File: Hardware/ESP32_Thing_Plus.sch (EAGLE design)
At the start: 43 parts, among them Q1 2.5A/30V, Q2 MBT3904DW1T1, U1 MCP73831, U2 ESP-WROOM-32NARROW, U3 AP2112K-3.3V, U4 CP2102N

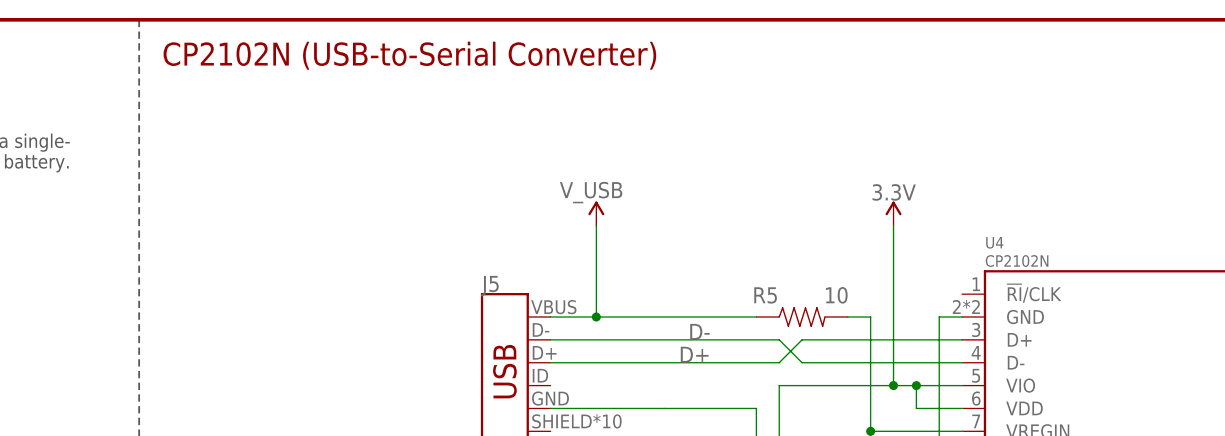
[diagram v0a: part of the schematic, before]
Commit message: Updated USB to UART converter
Updated shematic to indicate the USB to UART converter can be either the CP2104 or CP2102N
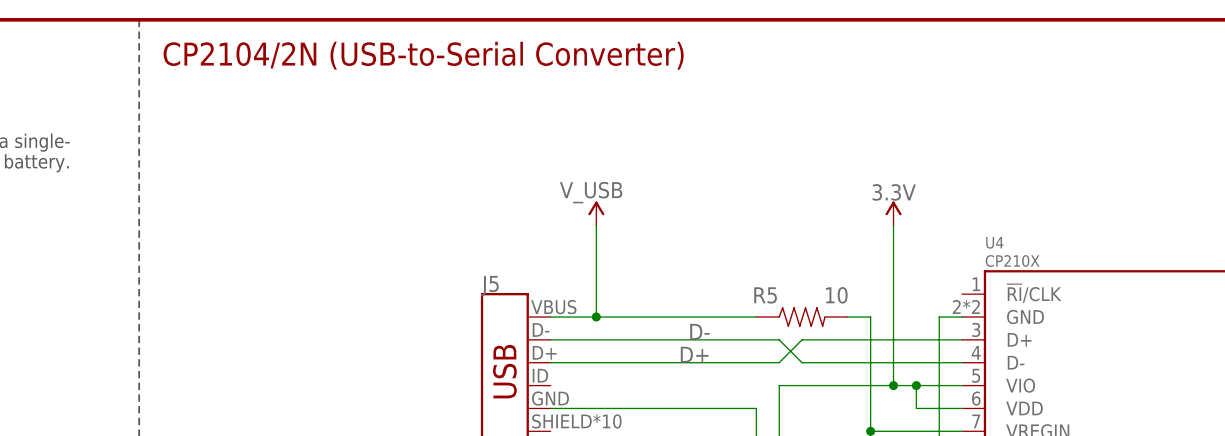
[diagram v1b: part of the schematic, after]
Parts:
- U4: value CP2102N -> CP210X
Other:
- note added: "CP2104/2N (USB-to-Serial Converter)"
- note removed: "CP2102N (USB-to-Serial Converter)"
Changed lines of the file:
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@@
 <part name="SUPPLY1" library="SparkFun-Aesthetics" deviceset="3.3V" device=""/>
 <part name="GND6" library="SparkFun-Aesthetics" deviceset="GND" device=""/>
-<part name="U4" library="SparkFun-IC-Comms" deviceset="CP2102N" device=""/>
+<part name="U4" library="SparkFun-IC-Comms" deviceset="CP2102N" device="" value="CP210X"/>
 <part name="R1" library="SparkFun-Resistors" deviceset="1KOHM" device="-0603-1/10W-1%" value="1k"/>
 <part name="SUPPLY9" library="SparkFun-PowerSymbols" deviceset="3.3V" device=""/>
@@
 If U0TXD, GPIO2, GPIO5 are floating,
 GPIO0 determines boot mode</text>
-<text x="256.54" y="274.32" size="2.54" layer="94" font="vector">CP2102N (USB-to-Serial Converter)</text>
+<text x="256.54" y="274.32" size="2.54" layer="94" font="vector">CP2104/2N (USB-to-Serial Converter)</text>
 <text x="246.38" y="266.7" size="1.524" layer="97" rot="MR0" align="top-left">V_BATT should be a single-
 cell LiPo battery.</text>

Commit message: Updated Attributes
Changed U2 Prod_ID from IC-13849 to IC-15676
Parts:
- U2: PROD_ID IC-13849 -> IC-15676
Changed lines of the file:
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@@
 <part name="J4" library="SparkFun-Connectors" deviceset="CONN_16" device="1X16_SM_SQ_NOSILK"/>
 <part name="U2" library="SparkFun-RF" deviceset="ESP-WROOM-32" device="NARROW">
-<attribute name="PROD_ID" value="IC-13849"/>
+<attribute name="PROD_ID" value="IC-15676"/>
 </part>
 <part name="SUPPLY3" library="SparkFun-Aesthetics" deviceset="V_BATT" device=""/>
